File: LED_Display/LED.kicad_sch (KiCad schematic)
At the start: 12 parts, among them U3 TPIC6C595N

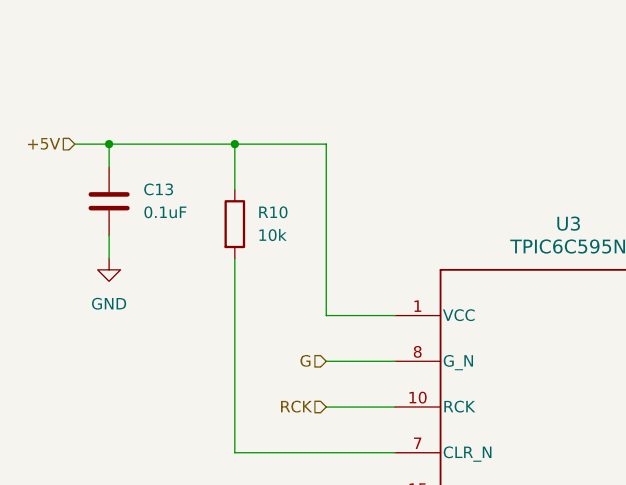
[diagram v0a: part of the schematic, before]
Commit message: Split_PCB
Split PCB to 1 piece / 1 file and start to layout
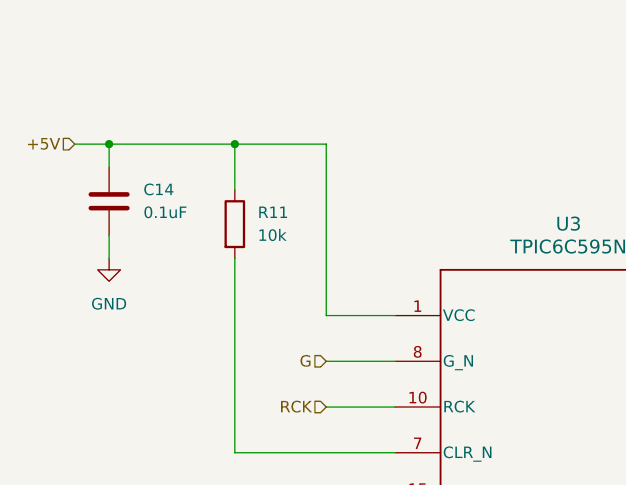
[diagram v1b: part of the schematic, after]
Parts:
- renumbered C13 to C14, R10 to R11
